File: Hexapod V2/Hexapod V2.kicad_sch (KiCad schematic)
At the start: 38 parts, among them J1 Battery, J3 OLED, U1 MPU6050, U2 NRF24L01_Breakout, U3 ACS712xLCTR-05B

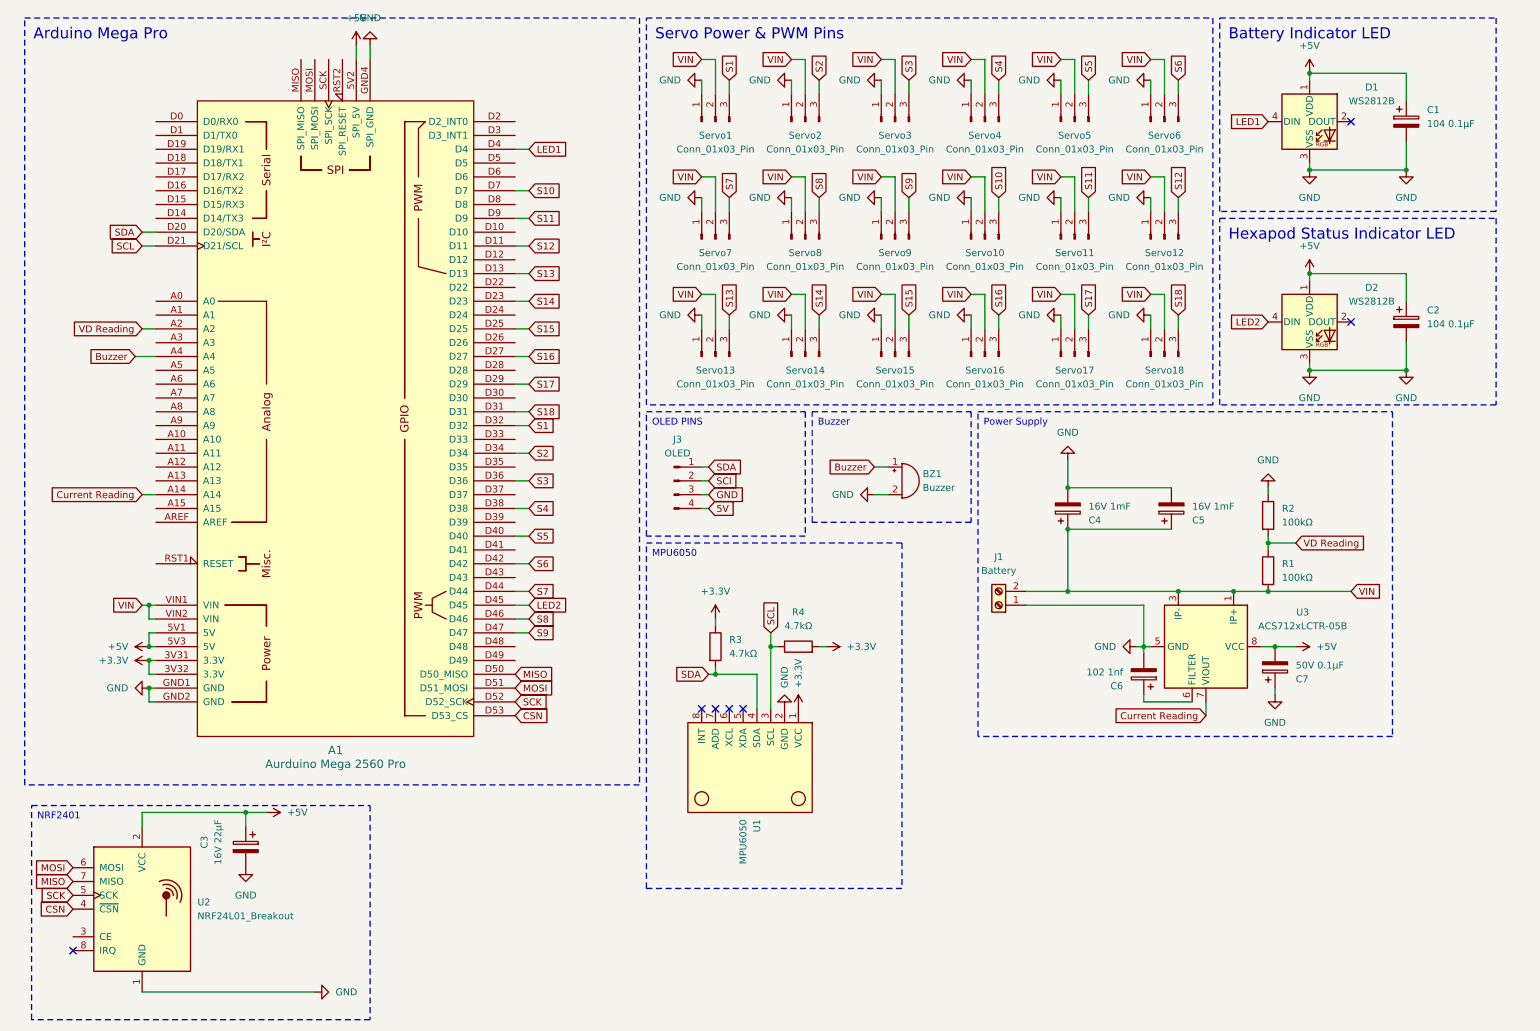
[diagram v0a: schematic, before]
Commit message: Added Teensy
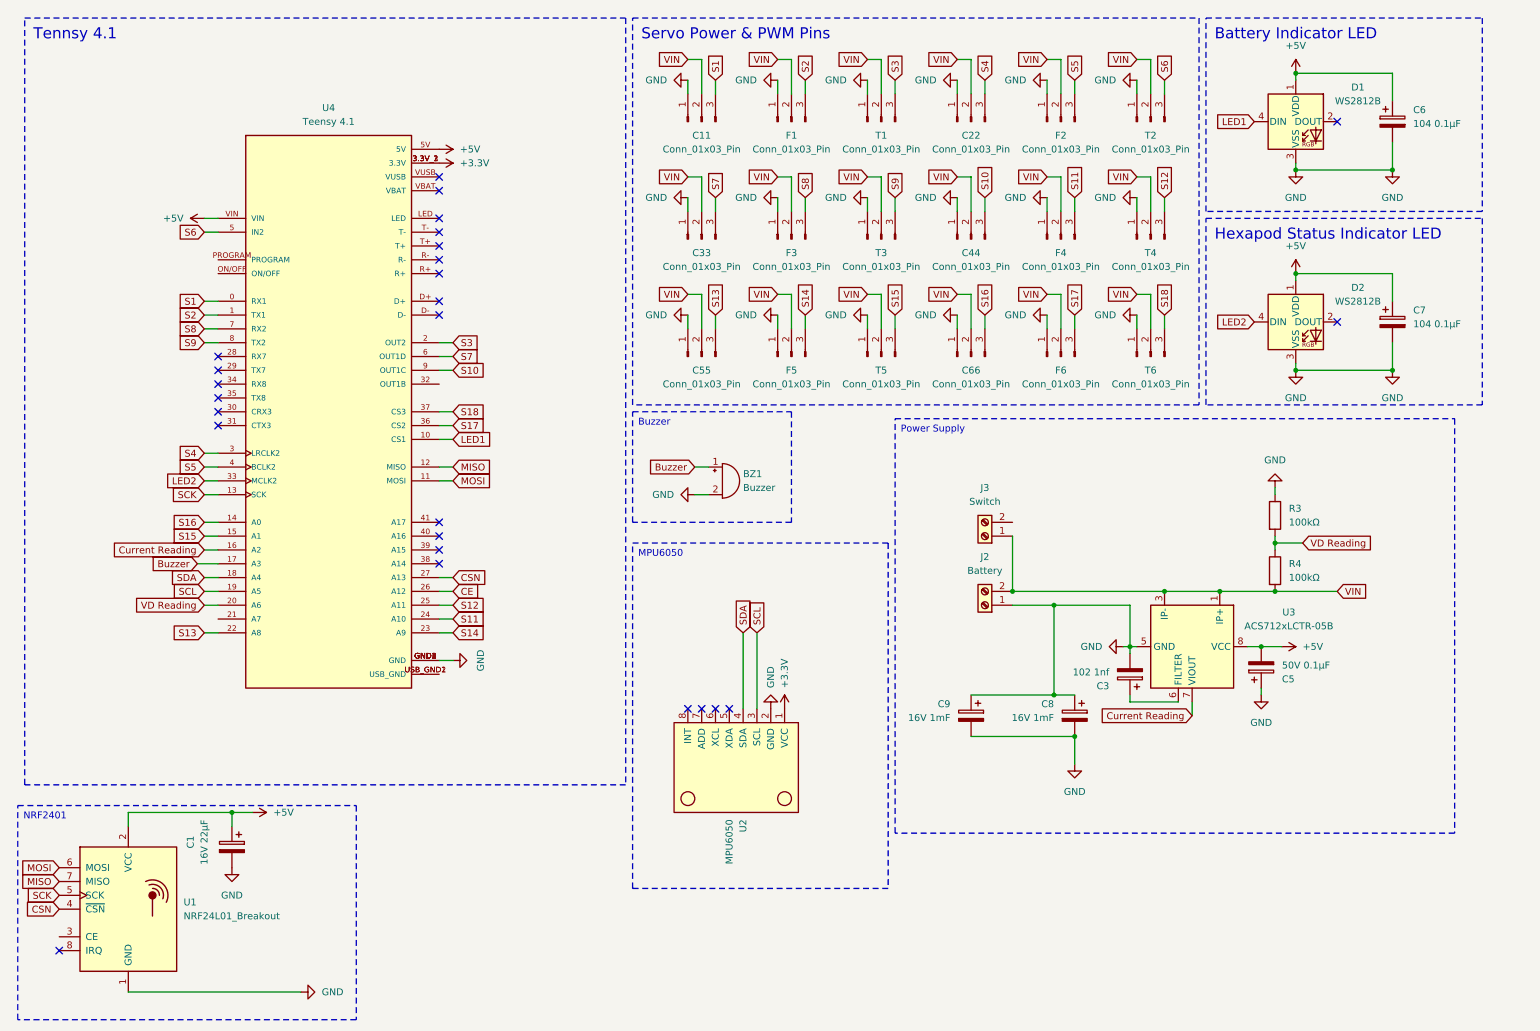
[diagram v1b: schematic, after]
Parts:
- removed A1: Aurduino Mega 2560 Pro, Arduino Library:Clone_Mega2560_Pro_Socket, symbol Arduino Library:Clone_Mega2560_Pro_Socket
- removed C2: 104 0.1μF, Capacitor_SMD:C_1206_3216Metric, symbol Device:C_Polarized
- removed C4: 16V 1mF, Capacitor_THT:CP_Radial_D10.0mm_P7.50mm, symbol Device:C_Polarized
- removed J1: Battery, TerminalBlock_Phoenix:TerminalBlock_Phoenix_MKDS-1,5-2-5.08_1x02_P5.08mm_Horizontal, symbol Connector:Screw_Terminal_01x02
- removed J3: OLED, symbol Connector:Conn_01x04_Pin
- removed R1, R2: 100kΩ, Resistor_THT:R_Axial_DIN0207_L6.3mm_D2.5mm_P7.62mm_Horizontal, symbol Device:R
- removed Servo1, Servo10, Servo11, Servo12, Servo13, Servo14, Servo15, Servo16, Servo17, Servo18, Servo2, Servo3, Servo4, Servo5, Servo6, Servo7, Servo8, Servo9: Conn_01x03_Pin, Connector_PinHeader_2.54mm:PinHeader_1x03_P2.54mm_Vertical, symbol Connector:Conn_01x03_Pin
- removed U1: MPU6050, usini_sensors:module_mpu6050, symbol Breakout Sensors:module_mpu6050
- removed U2: NRF24L01_Breakout, RF_Module:nRF24L01_Breakout, symbol RF:NRF24L01_Breakout
- added C11, C22, C33, C44, C55, C66, F1, F2, F3, F4, F5, F6, T1, T2, T3, T4, T5, T6: Conn_01x03_Pin, Connector_PinHeader_2.54mm:PinHeader_1x03_P2.54mm_Vertical, symbol Connector:Conn_01x03_Pin
- added C8, C9: 16V 1mF, Capacitor_THT:CP_Radial_D10.0mm_P7.50mm, symbol Device:C_Polarized
- added J2: Battery, TerminalBlock_Phoenix:TerminalBlock_Phoenix_MKDS-1,5-2-5.08_1x02_P5.08mm_Horizontal, symbol Connector:Screw_Terminal_01x02
- added J3: Switch, TerminalBlock_Phoenix:TerminalBlock_Phoenix_MKDS-1,5-2-5.08_1x02_P5.08mm_Horizontal, symbol Connector:Screw_Terminal_01x02
- added U1: NRF24L01_Breakout, RF_Module:nRF24L01_Breakout, symbol RF:NRF24L01_Breakout
- added U2: MPU6050, usini_sensors:module_mpu6050, symbol Breakout Sensors:module_mpu6050
- added U4: Teensy 4.1, usini_sensors:MODULE_DEV-16771, symbol DEV-16771:DEV-16771
- C1: value 104 0.1μF -> 16V 22μF; footprint Capacitor_SMD:C_1206_3216Metric -> Capacitor_THT:CP_Radial_D4.0mm_P2.00mm
- C3: value 16V 22μF -> 102 1nf; footprint Capacitor_THT:CP_Radial_D4.0mm_P2.00mm -> Capacitor_SMD:C_0805_2012Metric
- C5: value 16V 1mF -> 50V 0.1μF; footprint Capacitor_THT:CP_Radial_D10.0mm_P7.50mm -> Capacitor_SMD:C_0805_2012Metric
- C6: value 102 1nf -> 104 0.1μF; footprint Capacitor_SMD:C_0805_2012Metric -> Capacitor_SMD:C_1206_3216Metric
- C7: value 50V 0.1μF -> 104 0.1μF; footprint Capacitor_THT:CP_Radial_D5.0mm_P2.00mm -> Capacitor_SMD:C_1206_3216Metric
- R3, R4: value 4.7kΩ -> 100kΩ; footprint Resistor_SMD:R_1206_3216Metric -> Resistor_THT:R_Axial_DIN0207_L6.3mm_D2.5mm_P7.62mm_Horizontal
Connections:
- net +3.3V: now also U2.1 (VCC), U4.3.3V_1 (3.3V), U4.3.3V_2 (3.3V), U4.3.3V_3 (3.3V); no longer R3.1, R4.2
- net +5V: now also C5.2, C6.1, C7.1, U1.2 (VCC), U4.5V, U4.VIN; no longer C3.1, C7.2
- net Buzzer: now also U4.17 (A3)
- net CSN: now also U1.4 (~{CSN}), U4.27 (A13)
- net Current Reading: now also U4.16 (A2)
- net GND: now also C5.1, C7.2, R3.1, C11.1 (Pin_1), C22.1 (Pin_1), C33.1 (Pin_1), C44.1 (Pin_1), C55.1 (Pin_1), C66.1 (Pin_1), C8.1, C8.2, C9.1, C9.2, F1.1 (Pin_1), F2.1 (Pin_1), F3.1 (Pin_1), F4.1 (Pin_1), F5.1 (Pin_1), F6.1 (Pin_1), J2.1 (Pin_1), T1.1 (Pin_1), T2.1 (Pin_1), T3.1 (Pin_1), T4.1 (Pin_1), T5.1 (Pin_1), T6.1 (Pin_1), U1.1 (GND), U2.2 (GND), U4.GND1 (GND), U4.GND2 (GND), U4.GND3 (GND), U4.GND4 (GND), U4.GND5 (GND); no longer C5.2, C7.1
- net LED1: now also U4.10 (CS1)
- net LED2: now also U4.33 (MCLK2)
- net MISO: now also U1.7 (MISO), U4.12 (MISO)
- net MOSI: now also U1.6 (MOSI), U4.11 (MOSI)
- net S1: now also C11.3 (Pin_3), U4.0 (RX1)
- net S10: now also C44.3 (Pin_3), U4.9 (OUT1C)
- net S11: now also F4.3 (Pin_3), U4.24 (A10)
- net S12: now also T4.3 (Pin_3), U4.25 (A11)
- net S13: now also C55.3 (Pin_3), U4.22 (A8)
- net S14: now also F5.3 (Pin_3), U4.23 (A9)
- net S15: now also T5.3 (Pin_3), U4.15 (A1)
- net S16: now also C66.3 (Pin_3), U4.14 (A0)
- net S17: now also F6.3 (Pin_3), U4.36 (CS2)
- net S18: now also T6.3 (Pin_3), U4.37 (CS3)
- net S2: now also F1.3 (Pin_3), U4.1 (TX1)
- net S3: now also T1.3 (Pin_3), U4.2 (OUT2)
- net S4: now also C22.3 (Pin_3), U4.3 (LRCLK2)
- net S5: now also F2.3 (Pin_3), U4.4 (BCLK2)
- net S6: now also T2.3 (Pin_3), U4.5 (IN2)
- net S7: now also C33.3 (Pin_3), U4.6 (OUT1D)
- net S8: now also F3.3 (Pin_3), U4.7 (RX2)
- net S9: now also T3.3 (Pin_3), U4.8 (TX2)
- net SCK: now also U1.5 (SCK), U4.13 (SCK)
- net SCL: now also U2.3 (SCL), U4.19 (A5); no longer R4.1
- net SDA: now also U2.4 (SDA), U4.18 (A4); no longer R3.2
- net VD Reading: now also R3.2, R4.1, U4.20 (A6)
- net VIN: now also R4.2, C11.2 (Pin_2), C22.2 (Pin_2), C33.2 (Pin_2), C44.2 (Pin_2), C55.2 (Pin_2), C66.2 (Pin_2), F1.2 (Pin_2), F2.2 (Pin_2), F3.2 (Pin_2), F4.2 (Pin_2), F5.2 (Pin_2), F6.2 (Pin_2), J2.2 (Pin_2), J3.1 (Pin_1), T1.2 (Pin_2), T2.2 (Pin_2), T3.2 (Pin_2), T4.2 (Pin_2), T5.2 (Pin_2), T6.2 (Pin_2); no longer C5.1
- net at U3.6 (FILTER): now also C3.1; no longer C6.1
- new net: U4.USB_GND1 (USB_GND), U4.USB_GND2 (USB_GND)
- new net CE: U4.26 (A12)
- no-connect marks 7 -> 26
